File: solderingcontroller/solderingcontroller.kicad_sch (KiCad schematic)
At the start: 40 parts, among them J1 230V AC, Q3 BUZ11, Q4 BUZ11, SW1 HANDLE_DETECT, SW3 RotaryEncoder_Switch, T1 230/24, U1 ESP32-C3_SUPERMINI, U2 OLED LCD I2C, U3 16Bit I2C ADS1115 Module, U4 AMS1117-3.3, U5 MAX1044, U6 VOM1271T, U7 4N25

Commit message: Fix misstakes
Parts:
- added R13: 10k, symbol Device:R
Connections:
- net DETECT is gone; now on net DOCK_DETECT: SW1.2
- net +3V3: now also R13.1
- net AC1: no longer D3.1 (K)
- net DOCK_DETECT: now also R13.2
- net at R8.2, U7.1: now also D3.1 (K)
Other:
- moved on the sheet: D3, R8
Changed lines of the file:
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@@
 	)
 	(junction
-		(at 105.41 149.86)
+		(at 109.22 149.86)
 		(diameter 0)
 		(color 0 0 0 0)
@@
 	)
 	(junction
-		(at 105.41 142.24)
+		(at 109.22 142.24)
 		(diameter 0)
 		(color 0 0 0 0)
@@
 	(wire
 		(pts
+			(xy 106.68 142.24) (xy 109.22 142.24)
+		)
+		(stroke
+			(width 0)
+			(type default)
+		)
+	)
+	(wire
+		(pts
 			(xy 101.6 92.71) (xy 105.41 92.71)
 		)
@@
 	(wire
 		(pts
-			(xy 116.84 149.86) (xy 116.84 147.32)
+			(xy 121.92 149.86) (xy 121.92 147.32)
+		)
+		(stroke
+			(width 0)
+			(type default)
+		)
+	)
+	(wire
+		(pts
+			(xy 109.22 142.24) (xy 121.92 142.24)
 		)
 		(stroke
@@
 	(wire
 		(pts
-			(xy 100.33 149.86) (xy 105.41 149.86)
+			(xy 96.52 149.86) (xy 109.22 149.86)
 		)
 		(stroke
@@
 	(wire
 		(pts
-			(xy 118.11 142.24) (xy 121.92 142.24)
-		)
-		(stroke
-			(width 0)
-			(type default)
-		)
-	)
-	(wire
-		(pts
 			(xy 151.13 85.09) (xy 151.13 86.36)
 		)
@@
 	(wire
 		(pts
-			(xy 116.84 147.32) (xy 121.92 147.32)
-		)
-		(stroke
-			(width 0)
-			(type default)
-		)
-	)
-	(wire
-		(pts
 			(xy 138.43 97.79) (xy 144.78 97.79)
 		)
@@
 	(wire
 		(pts
-			(xy 105.41 142.24) (xy 110.49 142.24)
+			(xy 35.56 82.55) (xy 35.56 80.01)
 		)
 		(stroke
@@
 	(wire
 		(pts
-			(xy 35.56 82.55) (xy 35.56 80.01)
+			(xy 137.16 144.78) (xy 140.97 144.78)
 		)
 		(stroke
@@
 	(wire
 		(pts
-			(xy 137.16 144.78) (xy 140.97 144.78)
+			(xy 86.36 52.07) (xy 110.49 52.07)
 		)
 		(stroke
@@
 	(wire
 		(pts
-			(xy 100.33 142.24) (xy 105.41 142.24)
+			(xy 96.52 142.24) (xy 99.06 142.24)
 		)
 		(stroke
@@
 	(wire
 		(pts
-			(xy 105.41 149.86) (xy 116.84 149.86)
+			(xy 109.22 149.86) (xy 121.92 149.86)
 		)
 		(stroke
@@
 	)
 	(label "AC1"
-		(at 100.33 142.24 180)
+		(at 96.52 142.24 180)
 		(fields_autoplaced yes)
 		(effects
@@
 		)
 	)
-	(label "SENSEA{slash}V-"
+	(label "TC+{slash}V-"
 		(at 38.1 109.22 0)
 		(fields_autoplaced yes)
@@
 		)
 	)
-	(label "EARTH{slash}SENSEB"
+	(label "TC-{slash}EARTH"
 		(at 38.1 142.24 0)
 		(fields_autoplaced yes)
@@
 		)
 	)
-	(label "DETECT"
+	(label "DOCK_DETECT"
 		(at 55.88 133.35 0)
 		(fields_autoplaced yes)
@@
 		)
 	)
-	(label "SENSEA{slash}V-"
+	(label "TC+{slash}V-"
 		(at 101.6 92.71 180)
 		(fields_autoplaced yes)
@@
 	)
 	(label "AC2"
-		(at 100.33 149.86 180)
+		(at 96.52 149.86 180)
 		(fields_autoplaced yes)
 		(effects
@@
 		)
 	)
-	(label "EARTH{slash}SENSEB"
+	(label "TC-{slash}EARTH"
 		(at 101.6 114.3 180)
 		(fields_autoplaced yes)
@@
 		)
 	)
-	(label "SENSEA{slash}V-"
+	(label "TC+{slash}V-"
 		(at 109.22 187.96 0)
 		(fields_autoplaced yes)
@@
 	(symbol
 		(lib_id "Device:R")
-		(at 114.3 142.24 90)
+		(at 102.87 142.24 90)
 		(unit 1)
 		(exclude_from_sim no)
@@
 		(fields_autoplaced yes)
 		(property "Reference" "R8"
-			(at 114.3 135.89 90)
+			(at 102.87 135.89 90)
 			(effects
 				(font
@@
 		)
 		(property "Value" "3.3K"
-			(at 114.3 138.43 90)
+			(at 102.87 138.43 90)
 			(effects
 				(font
@@
 		)
 		(property "Footprint" ""
-			(at 114.3 144.018 90)
+			(at 102.87 144.018 90)
 			(effects
 				(font
@@
 		)
 		(property "Datasheet" "~"
-			(at 114.3 142.24 0)
+			(at 102.87 142.24 0)
 			(effects
 				(font
@@
 		)
 		(property "Description" "Resistor"
-			(at 114.3 142.24 0)
+			(at 102.87 142.24 0)
 			(effects
 				(font
@@
 	)
 	(symbol
+		(lib_id "Device:R")
+		(at 86.36 48.26 0)
+		(unit 1)
+		(exclude_from_sim no)
+		(in_bom yes)
+		(on_board yes)
+		(dnp no)
+		(fields_autoplaced yes)
+		(property "Reference" "R13"
+			(at 88.9 46.9899 0)
+			(effects
+				(font
+					(size 1.27 1.27)
+				)
+				(justify left)
+			)
+		)
+		(property "Value" "10k"
+			(at 88.9 49.5299 0)
+			(effects
+				(font
+					(size 1.27 1.27)
+				)
+				(justify left)
+			)
+		)
+		(property "Footprint" ""
+			(at 84.582 48.26 90)
+			(effects
+				(font
+					(size 1.27 1.27)
+				)
+				(hide yes)
+			)
+		)
+		(property "Datasheet" "~"
+			(at 86.36 48.26 0)
+			(effects
+				(font
+					(size 1.27 1.27)
+				)
+				(hide yes)
+			)
+		)
+		(property "Description" "Resistor"
+			(at 86.36 48.26 0)
+			(effects
+				(font
+					(size 1.27 1.27)
+				)
+				(hide yes)
+			)
+		)
+		(pin "2"
+		)
+		(pin "1"
+		)
+		(instances
+			(project "solderingcontroller"
+				(path "/9562c3ca-c9e5-4e2d-8a48-bcd20ff65be7"
+					(reference "R13")
+					(unit 1)
+				)
+			)
+		)
+	)
+	(symbol
 		(lib_id "power:GND")
 		(at 25.4 190.5 0)
@@
 	)
 	(symbol
+		(lib_id "power:+3V3")
+		(at 86.36 44.45 0)
+		(unit 1)
+		(exclude_from_sim no)
+		(in_bom yes)
+		(on_board yes)
+		(dnp no)
+		(fields_autoplaced yes)
+		(property "Reference" "#PWR026"
+			(at 86.36 48.26 0)
+			(effects
+				(font
+					(size 1.27 1.27)
+				)
+				(hide yes)
+			)
+		)
+		(property "Value" "+3V3"
+			(at 86.36 39.37 0)
+			(effects
+				(font
+					(size 1.27 1.27)
+				)
+			)
+		)
+		(property "Footprint" ""
+			(at 86.36 44.45 0)
+			(effects
+				(font
+					(size 1.27 1.27)
+				)
+				(hide yes)
+			)
+		)
+		(property "Datasheet" ""
+			(at 86.36 44.45 0)
+			(effects
+				(font
+					(size 1.27 1.27)
+				)
+				(hide yes)
+			)
+		)
+		(property "Description" "Power symbol creates a global label with name \"+3V3\""
+			(at 86.36 44.45 0)
+			(effects
+				(font
+					(size 1.27 1.27)
+				)
+				(hide yes)
+			)
+		)
+		(pin "1"
+		)
+		(instances
+			(project "solderingcontroller"
+				(path "/9562c3ca-c9e5-4e2d-8a48-bcd20ff65be7"
+					(reference "#PWR026")
+					(unit 1)
+				)
+			)
+		)
+	)
+	(symbol
 		(lib_id "Device:R")
 		(at 180.34 52.07 0)
@@
 	(symbol
 		(lib_id "Device:D")
-		(at 105.41 146.05 270)
+		(at 109.22 146.05 270)
 		(unit 1)
 		(exclude_from_sim no)
@@
 		(fields_autoplaced yes)
 		(property "Reference" "D3"
-			(at 107.95 144.7799 90)
+			(at 111.76 144.7799 90)
 			(effects
 				(font
@@
 		)
 		(property "Value" "BAV199"
-			(at 107.95 147.3199 90)
+			(at 111.76 147.3199 90)
 			(effects
 				(font
@@
 		)
 		(property "Footprint" ""
-			(at 105.41 146.05 0)
+			(at 109.22 146.05 0)
 			(effects
 				(font
@@
 		)
 		(property "Datasheet" "~"
-			(at 105.41 146.05 0)
+			(at 109.22 146.05 0)
 			(effects
 				(font
@@
 		)
 		(property "Description" "Diode"
-			(at 105.41 146.05 0)
+			(at 109.22 146.05 0)
 			(effects
 				(font
@@
 		)
 		(property "Sim.Device" "D"
-			(at 105.41 146.05 0)
+			(at 109.22 146.05 0)
 			(effects
 				(font
@@
 		)
 		(property "Sim.Pins" "1=K 2=A"
-			(at 105.41 146.05 0)
+			(at 109.22 146.05 0)
 			(effects
 				(font

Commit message: Update tc stuff
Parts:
- R1: value R -> 100k
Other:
- note added: "GAIN: 200X"
- note added: "Temperature (°C) -> Output Voltage (V). K Type TC 200X gain 0C -> 0.0V 50C -> 0.41V 100C -> 0.82V 150C -> 1.23V 200C -> 1.64V 250C -> 2.05V 300C -> 2.46V 350C -> 2.87V 400C -> 3.28V 450C -> 3.69V 500C -> 4.10V"
- note added: "non-inverting amplifier"
- moved on the sheet: R1, TH1
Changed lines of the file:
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@@
 	)
 	(junction
-		(at 198.12 140.97)
+		(at 220.98 140.97)
 		(diameter 0)
 		(color 0 0 0 0)
@@
 	(wire
 		(pts
-			(xy 198.12 151.13) (xy 198.12 157.48)
+			(xy 220.98 151.13) (xy 220.98 154.94)
 		)
 		(stroke
@@
 	(wire
 		(pts
-			(xy 198.12 140.97) (xy 189.23 140.97)
+			(xy 220.98 140.97) (xy 212.09 140.97)
 		)
 		(stroke
@@
 	(wire
 		(pts
-			(xy 189.23 140.97) (xy 189.23 102.87)
+			(xy 212.09 140.97) (xy 212.09 102.87)
 		)
 		(stroke
@@
 	(wire
 		(pts
-			(xy 189.23 102.87) (xy 232.41 102.87)
+			(xy 212.09 102.87) (xy 232.41 102.87)
 		)
 		(stroke
@@
 	(wire
 		(pts
-			(xy 198.12 140.97) (xy 198.12 143.51)
+			(xy 220.98 140.97) (xy 220.98 143.51)
 		)
 		(stroke
@@
 		)
 	)
+	(text "non-inverting amplifier"
+		(exclude_from_sim no)
+		(at 133.604 89.662 0)
+		(effects
+			(font
+				(size 1.27 1.27)
+			)
+		)
+	)
 	(text "Thermocouple Ampltifier"
 		(exclude_from_sim no)
@@
 		)
 	)
+	(text "Temperature (°C) -> Output Voltage (V). K Type TC 200X gain\n0C   -> 0.0V\n50C  -> 0.41V\n100C -> 0.82V\n150C -> 1.23V\n200C -> 1.64V\n250C -> 2.05V\n300C -> 2.46V\n350C -> 2.87V\n400C -> 3.28V\n450C -> 3.69V\n500C -> 4.10V"
+		(exclude_from_sim no)
+		(at 180.34 129.286 0)
+		(effects
+			(font
+				(size 1.27 1.27)
+			)
+		)
+	)
 	(text "MCU"
 		(exclude_from_sim no)
@@
 	(text "Ambient Temp"
 		(exclude_from_sim no)
-		(at 198.628 119.38 0)
+		(at 221.488 119.38 0)
+		(effects
+			(font
+				(size 1.27 1.27)
+			)
+		)
+	)
+	(text "GAIN: 200X"
+		(exclude_from_sim no)
+		(at 157.734 112.522 0)
 		(effects
 			(font
@@
 	(symbol
 		(lib_id "power:+3V3")
-		(at 198.12 133.35 0)
+		(at 220.98 133.35 0)
 		(unit 1)
 		(exclude_from_sim no)
@@
 		(fields_autoplaced yes)
 		(property "Reference" "#PWR08"
-			(at 198.12 137.16 0)
+			(at 220.98 137.16 0)
 			(effects
 				(font
@@
 		)
 		(property "Value" "+3V3"
-			(at 198.12 128.27 0)
+			(at 220.98 128.27 0)
 			(effects
 				(font
@@
 		)
 		(property "Footprint" ""
-			(at 198.12 133.35 0)
+			(at 220.98 133.35 0)
 			(effects
 				(font
@@
 		)
 		(property "Datasheet" ""
-			(at 198.12 133.35 0)
+			(at 220.98 133.35 0)
 			(effects
 				(font
@@
 		)
 		(property "Description" "Power symbol creates a global label with name \"+3V3\""
-			(at 198.12 133.35 0)
+			(at 220.98 133.35 0)
 			(effects
 				(font
@@
 	(symbol
 		(lib_id "Device:R")
-		(at 198.12 147.32 0)
+		(at 220.98 147.32 0)
 		(unit 1)
 		(exclude_from_sim no)
@@
 		(fields_autoplaced yes)
 		(property "Reference" "R1"
-			(at 200.66 146.0499 0)
+			(at 223.52 146.0499 0)
 			(effects
 				(font
@@
 			)
 		)
-		(property "Value" "R"
-			(at 200.66 148.5899 0)
+		(property "Value" "100k"
+			(at 223.52 148.5899 0)
 			(effects
 				(font
@@
 		)
 		(property "Footprint" ""
-			(at 196.342 147.32 90)
+			(at 219.202 147.32 90)
 			(effects
 				(font
@@
 		)
 		(property "Datasheet" "~"
-			(at 198.12 147.32 0)
+			(at 220.98 147.32 0)
 			(effects
 				(font
@@
 		)
 		(property "Description" "Resistor"
-			(at 198.12 147.32 0)
+			(at 220.98 147.32 0)
 			(effects
 				(font
@@
 	(symbol
 		(lib_id "power:GND")
-		(at 198.12 157.48 0)
+		(at 220.98 154.94 0)
 		(unit 1)
 		(exclude_from_sim no)
@@
 		(fields_autoplaced yes)
 		(property "Reference" "#PWR09"
-			(at 198.12 163.83 0)
+			(at 220.98 161.29 0)
 			(effects
 				(font
@@
 		)
 		(property "Value" "GND"
-			(at 198.12 162.56 0)
+			(at 220.98 160.02 0)
 			(effects
 				(font
@@
 		)
 		(property "Footprint" ""
-			(at 198.12 157.48 0)
+			(at 220.98 154.94 0)
 			(effects
 				(font
@@
 		)
 		(property "Datasheet" ""
-			(at 198.12 157.48 0)
+			(at 220.98 154.94 0)
 			(effects
 				(font
@@
 		)
 		(property "Description" "Power symbol creates a global label with name \"GND\" , ground"
-			(at 198.12 157.48 0)
+			(at 220.98 154.94 0)
 			(effects
 				(font
@@
 	(symbol
 		(lib_id "Device:Thermistor_NTC")
-		(at 198.12 137.16 0)
+		(at 220.98 137.16 0)
 		(unit 1)
 		(exclude_from_sim no)
@@
 		(fields_autoplaced yes)
 		(property "Reference" "TH1"
-			(at 200.66 136.2074 0)
+			(at 223.52 136.2074 0)
 			(effects
 				(font
@@
 		)
 		(property "Value" "Thermistor_NTC 100K"
-			(at 200.66 138.7474 0)
+			(at 223.52 138.7474 0)
 			(effects
 				(font
@@
 		)
 		(property "Footprint" ""
-			(at 198.12 135.89 0)
+			(at 220.98 135.89 0)
 			(effects
 				(font
@@
 		)
 		(property "Datasheet" "~"
-			(at 198.12 135.89 0)
+			(at 220.98 135.89 0)
 			(effects
 				(font
@@
 		)
 		(property "Description" "Temperature dependent resistor, negative temperature coefficient"
-			(at 198.12 137.16 0)
+			(at 220.98 137.16 0)
 			(effects
 				(font

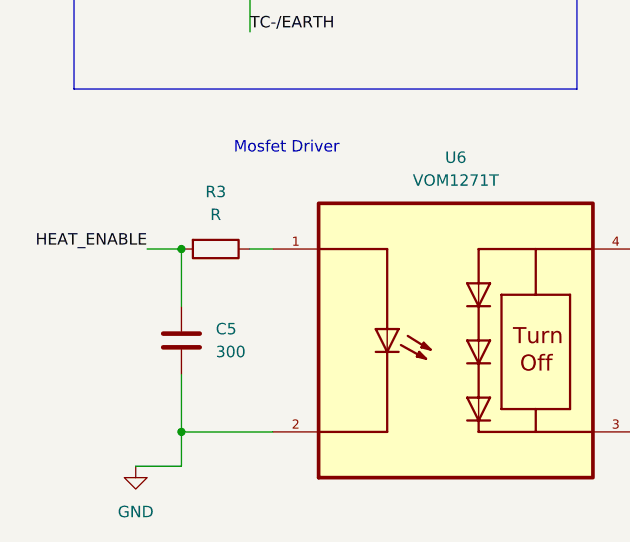
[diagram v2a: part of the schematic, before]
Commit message: Update missing values
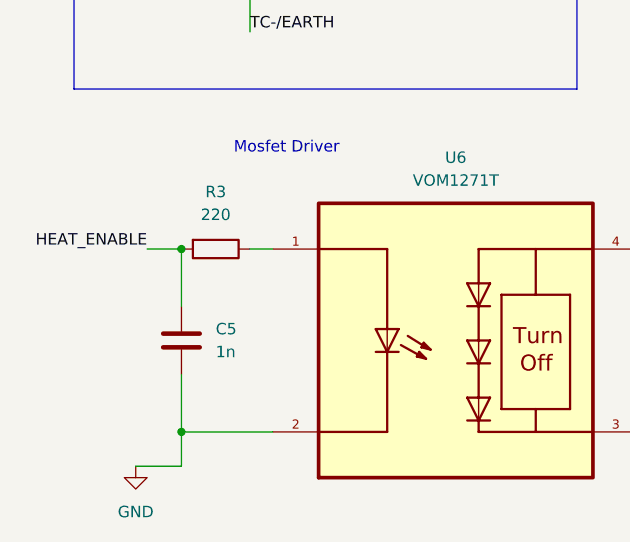
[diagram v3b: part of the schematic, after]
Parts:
- C5: value 300 -> 1n
- R3: value R -> 220
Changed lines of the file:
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@@
 			)
 		)
-		(property "Value" "300"
+		(property "Value" "1n"
 			(at 34.29 177.7999 0)
 			(effects
@@
 			)
 		)
-		(property "Value" "R"
+		(property "Value" "220"
 			(at 34.29 162.56 90)
 			(effects

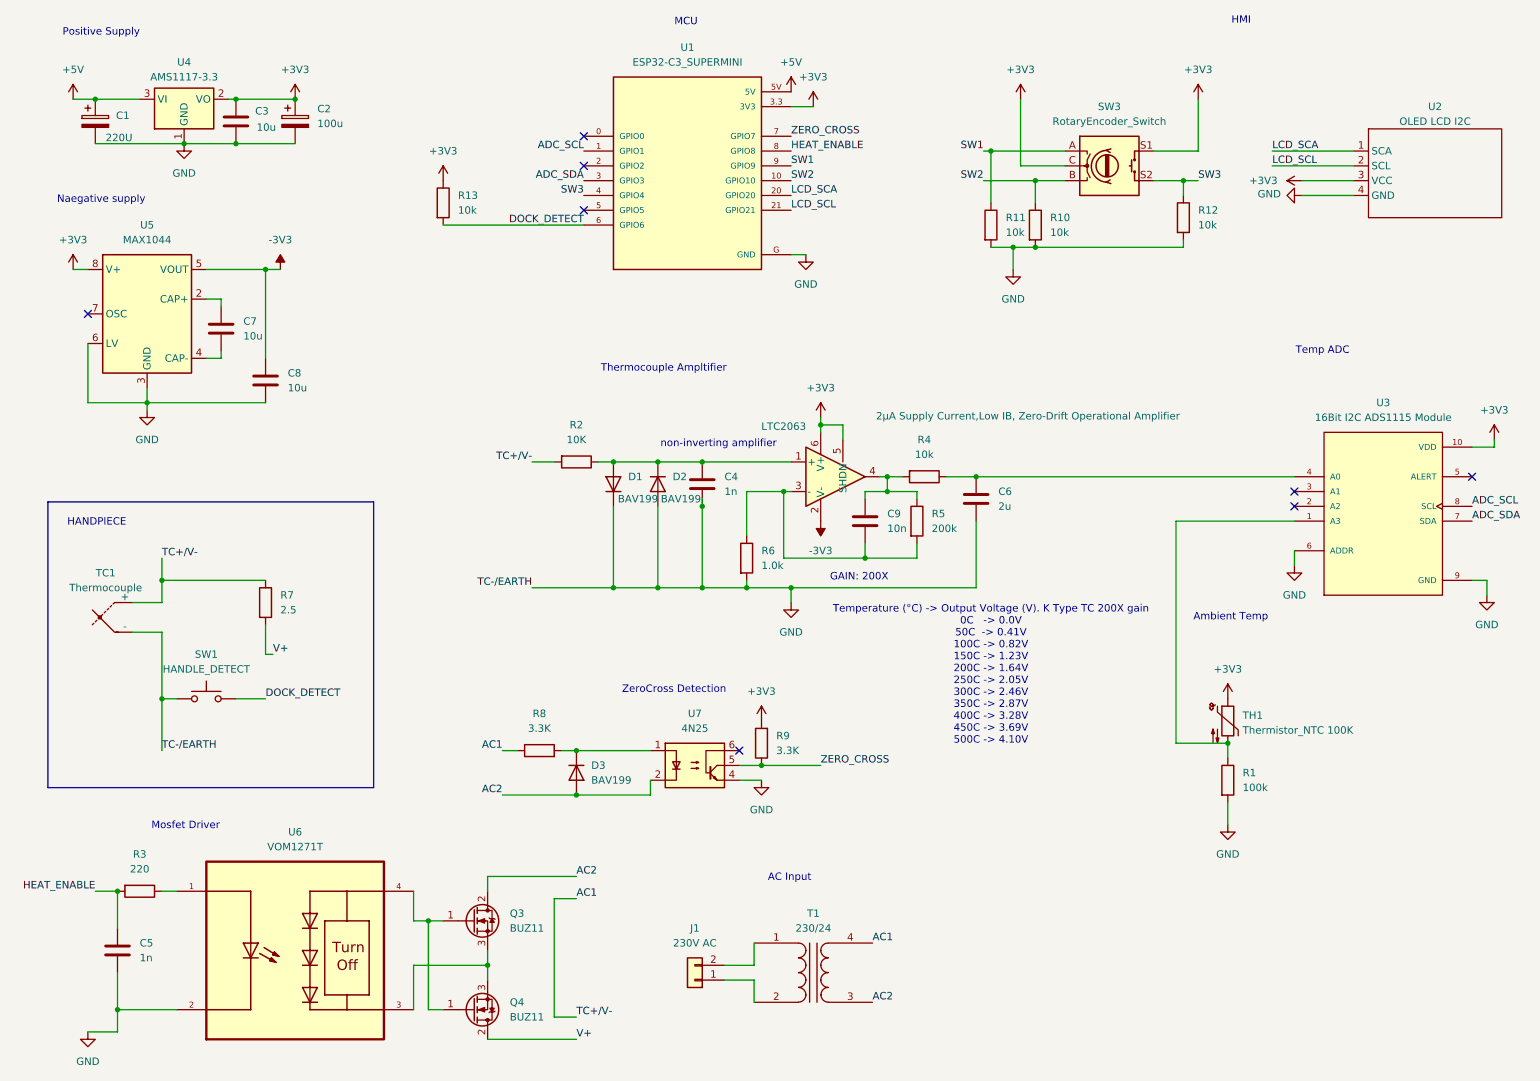
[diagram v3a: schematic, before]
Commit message: Simplify schematic
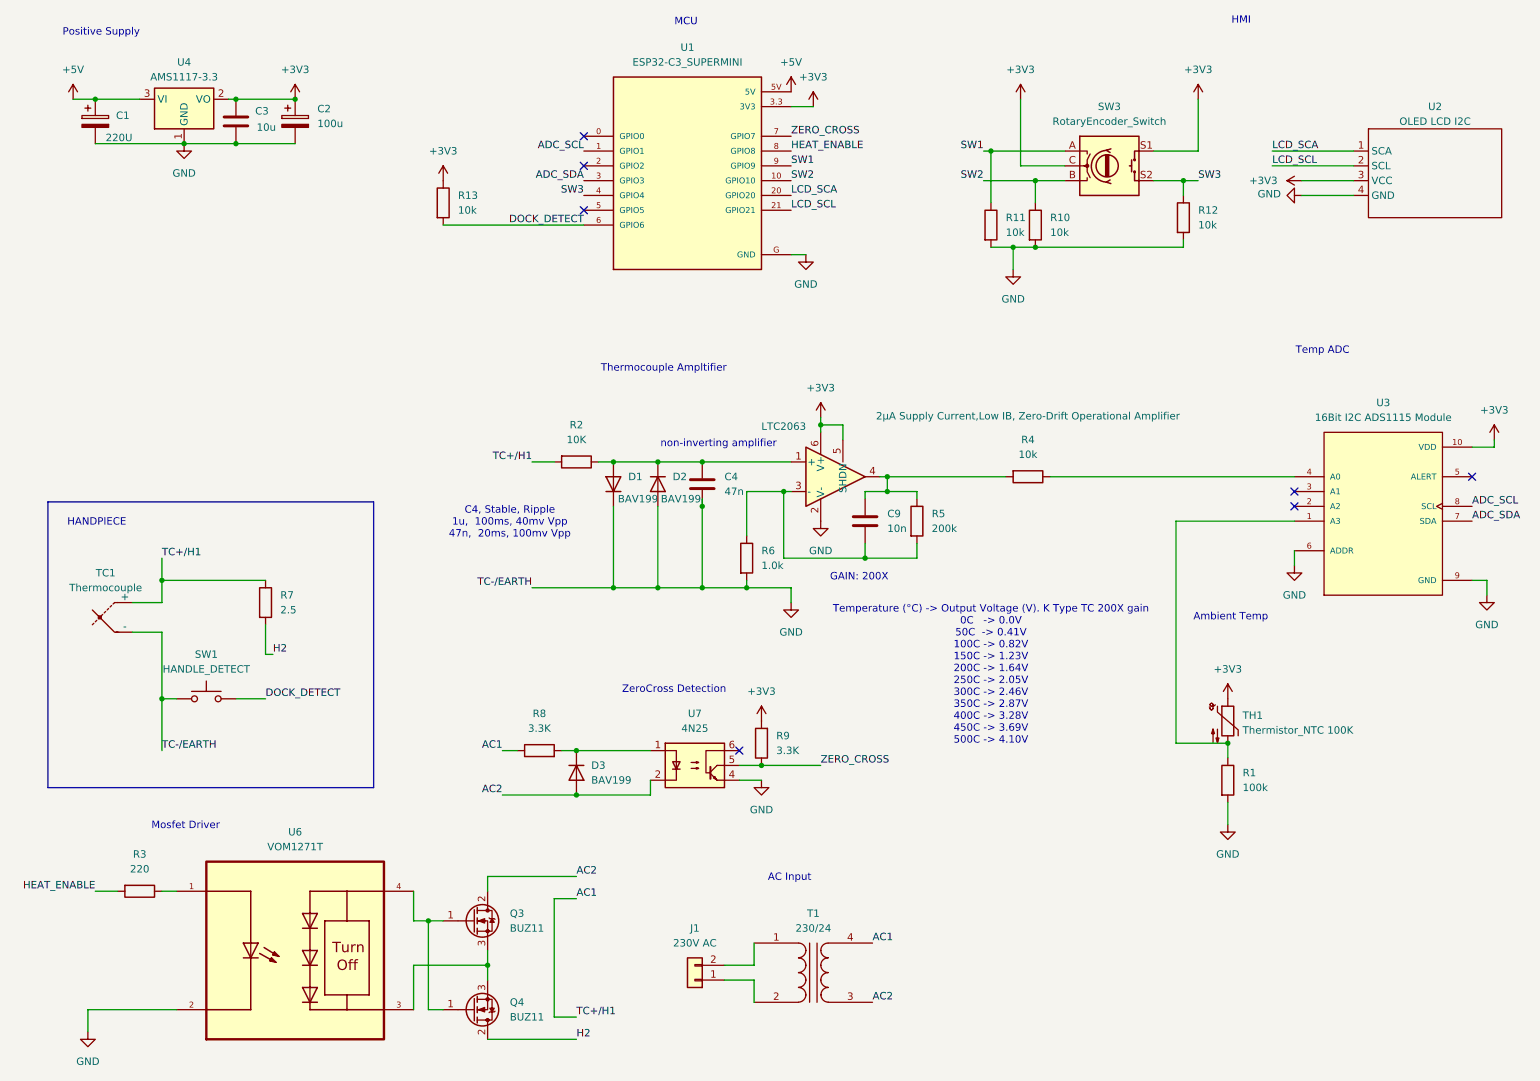
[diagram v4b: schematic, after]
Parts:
- removed C5: 1n, symbol Device:C
- removed C6: 2u, symbol Device:C
- removed C7, C8: 10u, symbol Device:C
- removed U5: MAX1044, symbol Regulator_SwitchedCapacitor:MAX1044
- C4: value 1n -> 47n
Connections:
- net -3V3 is gone; now on net GND: LTC2063.2 (V-)
- net V+ renamed H2
- no-connect marks 8 -> 7
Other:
- note added: "C4, Stable, Ripple 1u, 100ms, 40mv Vpp 47n, 20ms, 100mv Vpp"
- note removed: "Naegative supply"
- moved on the sheet: R4

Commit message: Update
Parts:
- removed R10, R11, R12: 10k, symbol Device:R
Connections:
- net +3V3: no longer SW3.C, SW3.S1
- net GND: now also SW3.C, SW3.S1

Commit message: Update
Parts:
- R7: value 2.5 -> 11.5
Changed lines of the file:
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@@
 			)
 		)
-		(property "Value" "2.5"
+		(property "Value" "11.5"
 			(at 58.42 118.1099 0)
 			(effects
